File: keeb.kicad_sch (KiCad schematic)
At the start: 20 parts, among them J1 AVR-ISP-6, SW1 SW_MEC_5E, U1 ATmega32U4-A, Y1 16 Mhz XTAL

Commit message: changed to 60 :C
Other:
- removed sheet rgbSideglow
- note removed: "RGB Sideglow"

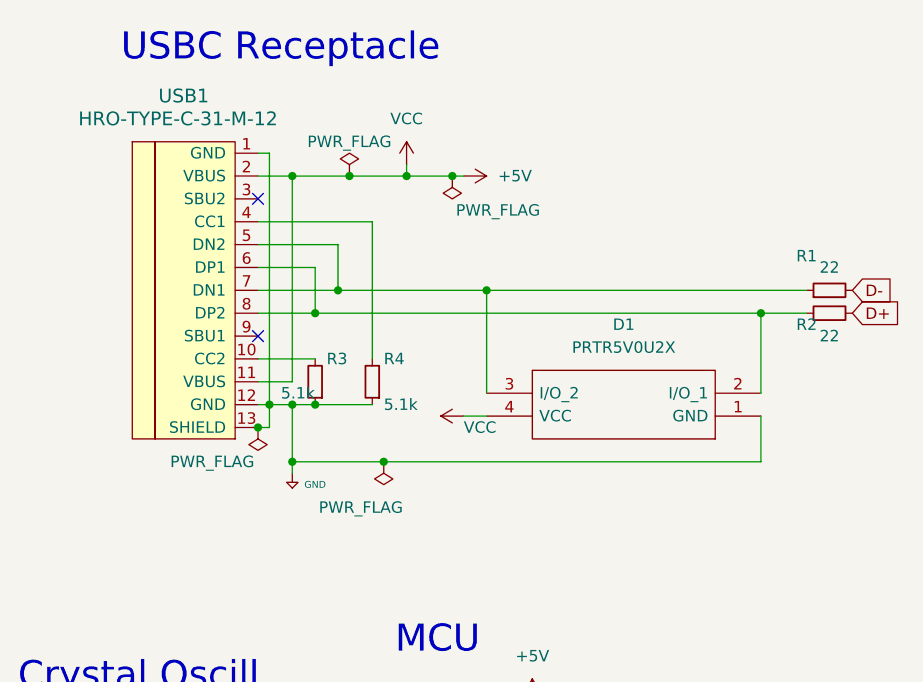
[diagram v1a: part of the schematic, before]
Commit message: moved keys/neopixels
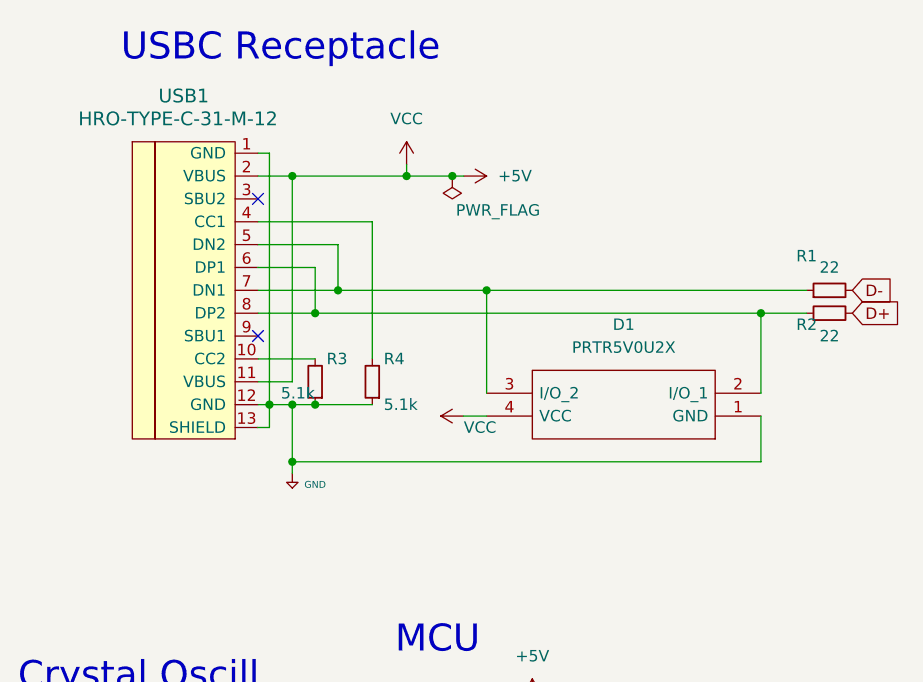
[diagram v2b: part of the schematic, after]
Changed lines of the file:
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@@
   (junction (at 27.94 167.64) (diameter 0) (color 0 0 0 0)
   )
-  (junction (at 43.18 66.04) (diameter 0) (color 0 0 0 0)
-  )
-  (junction (at 57.15 69.85) (diameter 0) (color 0 0 0 0)
-  )
   (junction (at 27.94 172.72) (diameter 0) (color 0 0 0 0)
   )
@@
   )
   (junction (at 46.99 69.85) (diameter 0) (color 0 0 0 0)
-  )
-  (junction (at 53.34 38.1) (diameter 0) (color 0 0 0 0)
   )
   (junction (at 33.02 167.64) (diameter 0) (color 0 0 0 0)
@@
     (stroke (width 0) (type default) (color 0 0 0 0))
   )
-  (wire (pts (xy 46.99 38.1) (xy 53.34 38.1))
-    (stroke (width 0) (type default) (color 0 0 0 0))
-  )
   (wire (pts (xy 27.94 172.72) (xy 33.02 172.72))
     (stroke (width 0) (type default) (color 0 0 0 0))
@@
     (stroke (width 0) (type default) (color 0 0 0 0))
   )
-  (wire (pts (xy 57.15 69.85) (xy 46.99 69.85))
-    (stroke (width 0) (type default) (color 0 0 0 0))
-  )
-  (wire (pts (xy 53.34 38.1) (xy 59.69 38.1))
+  (wire (pts (xy 46.99 38.1) (xy 59.69 38.1))
     (stroke (width 0) (type default) (color 0 0 0 0))
   )
@@
     (stroke (width 0) (type default) (color 0 0 0 0))
   )
-  (wire (pts (xy 99.06 69.85) (xy 57.15 69.85))
+  (wire (pts (xy 46.99 69.85) (xy 99.06 69.85))
     (stroke (width 0) (type default) (color 0 0 0 0))
   )
@@
     (pin "1")
   )
-  (symbol (lib_id "power:PWR_FLAG") (at 43.18 66.04 180) (unit 1)
-    (in_bom yes) (on_board yes)
-    (property "Reference" "#FLG03" (id 0) (at 43.18 67.945 0)
-      (effects (font (size 1.27 1.27)) hide)
-    )
-    (property "Value" "PWR_FLAG" (id 1) (at 38.1 69.85 0))
-    (property "Footprint" "" (id 2) (at 43.18 66.04 0)
-      (effects (font (size 1.27 1.27)) hide)
-    )
-    (property "Datasheet" "~" (id 3) (at 43.18 66.04 0)
-      (effects (font (size 1.27 1.27)) hide)
-    )
-    (pin "1")
-  )
   (symbol (lib_id "keyboard_parts:GND") (at 120.65 128.27 0) (unit 1)
     (in_bom yes) (on_board yes) (fields_autoplaced)
@@
     (pin "1")
   )
-  (symbol (lib_id "power:PWR_FLAG") (at 57.15 69.85 180) (unit 1)
-    (in_bom yes) (on_board yes)
-    (property "Reference" "#FLG04" (id 0) (at 57.15 71.755 0)
-      (effects (font (size 1.27 1.27)) hide)
-    )
-    (property "Value" "PWR_FLAG" (id 1) (at 54.61 74.93 0))
-    (property "Footprint" "" (id 2) (at 57.15 69.85 0)
-      (effects (font (size 1.27 1.27)) hide)
-    )
-    (property "Datasheet" "~" (id 3) (at 57.15 69.85 0)
-      (effects (font (size 1.27 1.27)) hide)
-    )
-    (pin "1")
-  )
   (symbol (lib_id "keyboard_parts:GND") (at 107.95 158.75 0) (unit 1)
     (in_bom yes) (on_board yes)
@@
     (pin "1")
     (pin "2")
-  )
-  (symbol (lib_id "power:PWR_FLAG") (at 53.34 38.1 0) (unit 1)
-    (in_bom yes) (on_board yes)
-    (property "Reference" "#FLG01" (id 0) (at 53.34 36.195 0)
-      (effects (font (size 1.27 1.27)) hide)
-    )
-    (property "Value" "PWR_FLAG" (id 1) (at 53.34 34.29 0))
-    (property "Footprint" "" (id 2) (at 53.34 38.1 0)
-      (effects (font (size 1.27 1.27)) hide)
-    )
-    (property "Datasheet" "~" (id 3) (at 53.34 38.1 0)
-      (effects (font (size 1.27 1.27)) hide)
-    )
-    (pin "1")
   )
   (symbol (lib_id "power:+5V") (at 127 158.75 0) (unit 1)
@@
   )
   (symbol_instances
-    (path "/7ab60663-f1e4-44f9-9045-1c753b730dc9"
-      (reference "#FLG01") (unit 1) (value "PWR_FLAG") (footprint "")
-    )
     (path "/1bf8731a-d8b6-461d-80b4-9a68bc5acb37"
       (reference "#FLG02") (unit 1) (value "PWR_FLAG") (footprint "")
     )
-    (path "/39702c22-919b-40ad-9e63-11613ac268af"
-      (reference "#FLG03") (unit 1) (value "PWR_FLAG") (footprint "")
-    )
-    (path "/51a57b28-cfe7-4f9a-9d71-5d4ea21a51d2"
-      (reference "#FLG04") (unit 1) (value "PWR_FLAG") (footprint "")
-    )
     (path "/f4c88423-dd40-4310-83fa-b3433012d8d3"
       (reference "#PWR01") (unit 1) (value "VCC") (footprint "")
@@
       (reference "#PWR0146") (unit 1) (value "+5V") (footprint "")
     )
-    (path "/40940281-55a3-43d0-8f01-7316aa0f04ca/94e1acdc-e4a0-451a-9165-bba7cb4ed5e6"
-      (reference "#PWR0147") (unit 1) (value "+5V") (footprint "")
-    )
     (path "/40940281-55a3-43d0-8f01-7316aa0f04ca/fce2a4a3-26a9-4d43-b7b0-8a1cd935d8be"
       (reference "#PWR0148") (unit 1) (value "GND") (footprint "")
@@
       (reference "#PWR0156") (unit 1) (value "GND") (footprint "")
     )
-    (path "/40940281-55a3-43d0-8f01-7316aa0f04ca/5167347e-3f74-4935-a136-b6422d046948"
-      (reference "#PWR0157") (unit 1) (value "GND") (footprint "")
-    )
     (path "/40940281-55a3-43d0-8f01-7316aa0f04ca/9385b162-5519-45af-b62d-19d8056ffddb"
       (reference "#PWR0158") (unit 1) (value "GND") (footprint "")
@@
       (reference "C75") (unit 1) (value "100nF") (footprint "Capacitor_SMD:C_0805_2012Metric_Pad1.18x1.45mm_HandSolder")
     )
-    (path "/40940281-55a3-43d0-8f01-7316aa0f04ca/5e44bb64-7c02-4689-9ab6-86cfc8ff36c0"
-      (reference "C76") (unit 1) (value "100nF") (footprint "Capacitor_SMD:C_0805_2012Metric_Pad1.18x1.45mm_HandSolder")
-    )
     (path "/e9764993-7462-40fd-8d4b-02d010ee99fe"
       (reference "D1") (unit 1) (value "PRTR5V0U2X") (footprint "random-keyboard-parts2:SOT143B")
@@
       (reference "D68") (unit 1) (value "SK6812MINI") (footprint "LED_SMD:LED_SK6812MINI_PLCC4_3.5x3.5mm_P1.75mm")
     )
-    (path "/40940281-55a3-43d0-8f01-7316aa0f04ca/ce4e679f-230d-44ef-97d5-f59854a4fc2a"
-      (reference "D69") (unit 1) (value "SK6812MINI") (footprint "LED_SMD:LED_SK6812MINI_PLCC4_3.5x3.5mm_P1.75mm")
-    )
     (path "/39dabec8-ee69-4816-aadc-d8efa99bb3bd/ac9af6dd-8fcf-4bb0-9640-f5906983d6ee"
       (reference "D94") (unit 1) (value "D_Small") (footprint "Diode_SMD:D_SOD-123")
@@
       (reference "D160") (unit 1) (value "D_Small") (footprint "Diode_SMD:D_SOD-123")
     )
-    (path "/39dabec8-ee69-4816-aadc-d8efa99bb3bd/254d2bc2-c5ab-4ad2-845c-3b28cd5df36e"
-      (reference "D161") (unit 1) (value "D_Small") (footprint "Diode_SMD:D_SOD-123")
-    )
     (path "/12e874c0-cb7a-483a-b94a-6167aca1e308"
       (reference "J1") (unit 1) (value "AVR-ISP-6") (footprint "random-keyboard-parts2:Reset_Pretty-Mask")
@@
       (reference "SW68") (unit 1) (value "SW_Push") (footprint "acheron_MXH:MX100H")
     )
-    (path "/39dabec8-ee69-4816-aadc-d8efa99bb3bd/ff89f079-3954-42f9-8254-d99af467a0a6"
-      (reference "SW69") (unit 1) (value "SW_Push") (footprint "acheron_MXH:MX100H")
-    )
     (path "/cc3d3d36-89c7-419a-8b9a-60591d414fb9"

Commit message: strange short?
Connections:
- net RESET: no longer SW1.4 (A)
- net ROW7: no longer names the net of U1.19 (PD1)
- net ROW8: no longer names the net of U1.20 (PD2)
- no-connect marks 3 -> 6

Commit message: began routing for real
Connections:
- net +5V: no longer C1.2, C2.2, C3.2, C4.2, C5.2, C6.2, C7.2, C8.2, D1.1 (GND), J1.6 (GND), R3.1, R4.1, R6.1, SW1.1, SW1.2, U1.15 (GND), U1.23 (GND), U1.35 (GND), U1.43 (GND), U1.5 (UGND), USB1.1 (GND), USB1.12 (GND), USB1.13 (SHIELD), Y1.2, Y1.4
- net COL0: now also U1.38 (PF5); no longer U1.21 (PD3)
- net COL2: now also U1.21 (PD3); no longer U1.22 (PD5)
- net COL9: now also U1.19 (PD1); no longer U1.38 (PF5)
- net MISO: now also U1.10 (PB2); no longer U1.11 (PB3)
- net MOSI: now also U1.11 (PB3); no longer U1.10 (PB2)
- net RE1: now also U1.20 (PD2); no longer U1.37 (PF6)
- net RE2: now also U1.18 (PD0); no longer U1.36 (PF7)
- net RESET: now also SW1.4 (A)
- net ROW3: now also U1.9 (PB1); no longer U1.12 (PB7)
- net ROW6: now also U1.22 (PD5); no longer U1.18 (PD0)
- net SCK: now also U1.12 (PB7); no longer U1.9 (PB1)
- new net GND: C1.2, C2.2, C3.2, C4.2, C5.2, C6.2, C7.2, C8.2, D1.1 (GND), J1.6 (GND), R3.1, R4.1, R6.1, SW1.1, SW1.2, U1.15 (GND), U1.23 (GND), U1.35 (GND), U1.43 (GND), U1.5 (UGND), USB1.1 (GND), USB1.12 (GND), USB1.13 (SHIELD), Y1.2, Y1.4
- no-connect marks 6 -> 3

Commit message: progress with redoing
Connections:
- no-connect marks 3 -> 5
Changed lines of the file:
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@@
   (junction (at 76.2 96.52) (diameter 0) (color 0 0 0 0)
   )
+  (no_connect (at 91.44 175.26))
+  (no_connect (at 91.44 177.8))
   (no_connect (at 43.18 40.64))
   (no_connect (at 43.18 55.88))
